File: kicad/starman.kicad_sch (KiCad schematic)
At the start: 202 parts, among them J1 Conn_01x12, J10 Barrel_Jack_MountingPin, J2 Conn_01x10, J3 Conn_01x12, J4 Conn_01x06, J5 Conn_02x03_Counter_Clockwise, J6 Conn_01x12, J7 Conn_01x10, J8 Conn_01x12, J9 Conn_01x08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

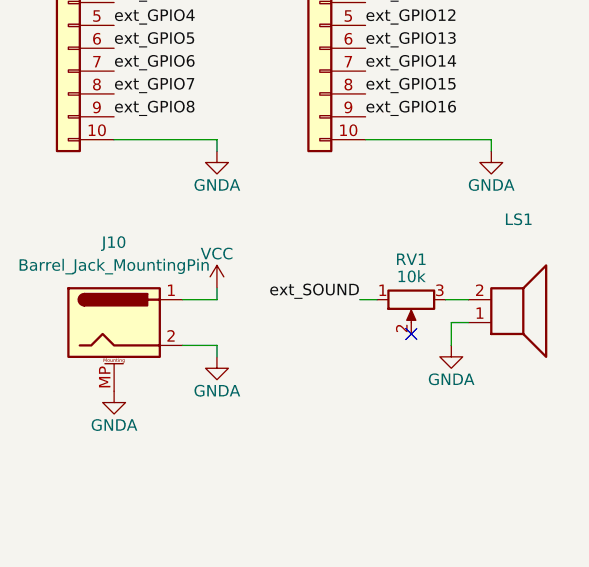
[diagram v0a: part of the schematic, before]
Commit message: Added some neat logos, fixed potentiometer
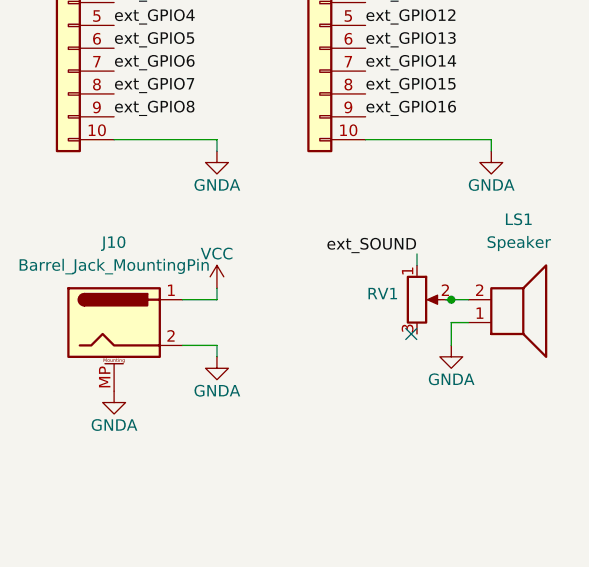
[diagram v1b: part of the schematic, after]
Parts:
- LS1: value (none) -> Speaker; footprint (none) -> Buzzer_Beeper:MagneticBuzzer_StarMicronics_HMB-06_HMB-12
- RV1: value 10k -> (none); footprint Potentiometer_SMD:Potentiometer_ACP_CA9-VSMD_Vertical -> (none)
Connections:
- net at LS1.2: now also RV1.2; no longer RV1.3
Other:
- moved on the sheet: RV1
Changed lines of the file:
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@@
   (junction (at 144.78 176.53) (diameter 0) (color 0 0 0 0)
   )
+  (junction (at 412.115 148.59) (diameter 0) (color 0 0 0 0)
+  )
   (junction (at 154.94 87.63) (diameter 0) (color 0 0 0 0)
   )
@@
     (stroke (width 0) (type default) (color 0 0 0 0))
   )
-  (wire (pts (xy 411.48 148.59) (xy 414.02 148.59))
+  (wire (pts (xy 411.48 148.59) (xy 412.115 148.59))
     (stroke (width 0) (type default) (color 0 0 0 0))
   )
@@
     (stroke (width 0) (type default) (color 0 0 0 0))
   )
+  (wire (pts (xy 412.115 148.59) (xy 414.02 148.59))
+    (stroke (width 0) (type default) (color 0 0 0 0))
+  )
   (wire (pts (xy 116.84 73.66) (xy 134.62 73.66))
     (stroke (width 0) (type default) (color 0 0 0 0))
@@
     (stroke (width 0) (type default) (color 0 0 0 0))
   )
+  (wire (pts (xy 408.305 143.51) (xy 408.305 144.78))
+    (stroke (width 0) (type default) (color 0 0 0 0))
+  )
   (wire (pts (xy 151.13 68.58) (xy 151.13 66.04))
     (stroke (width 0) (type default) (color 0 0 0 0))
@@
     (stroke (width 0) (type default) (color 0 0 0 0))
   )
-  (wire (pts (xy 401.955 148.59) (xy 403.86 148.59))
-    (stroke (width 0) (type default) (color 0 0 0 0))
-  )
   (wire (pts (xy 78.74 143.51) (xy 78.74 146.05))
     (stroke (width 0) (type default) (color 0 0 0 0))
@@
     (effects (font (size 1.27 1.27)) (justify left bottom))
   )
-  (label "ext_SOUND" (at 401.955 148.59 180)
+  (label "ext_SOUND" (at 408.305 143.51 180)
     (effects (font (size 1.27 1.27)) (justify right bottom))
   )
@@
     (in_bom yes) (on_board yes) (fields_autoplaced)
     (property "Reference" "LS1" (id 0) (at 419.608 139.7 0))
-    (property "Value" "" (id 1) (at 419.608 142.24 0))
-    (property "Footprint" "" (id 2) (at 419.1 146.05 0)
+    (property "Value" "Speaker" (id 1) (at 419.608 142.24 0))
+    (property "Footprint" "Buzzer_Beeper:MagneticBuzzer_StarMicronics_HMB-06_HMB-12" (id 2) (at 419.1 146.05 0)
       (effects (font (size 1.27 1.27)) hide)
     )
@@
     (pin "1")
   )
-  (symbol (lib_id "Device:R_Potentiometer") (at 407.67 148.59 90) (mirror x) (unit 1)
+  (symbol (lib_id "Device:R_Potentiometer") (at 408.305 148.59 0) (unit 1)
     (in_bom yes) (on_board yes)
-    (property "Reference" "RV1" (id 0) (at 407.67 144.145 90))
-    (property "Value" "10k" (id 1) (at 407.67 146.05 90))
-    (property "Footprint" "Potentiometer_SMD:Potentiometer_ACP_CA9-VSMD_Vertical" (id 2) (at 407.67 148.59 0)
+    (property "Reference" "RV1" (id 0) (at 404.495 147.955 0))
+    (property "Value" "" (id 1) (at 404.495 149.86 0))
+    (property "Footprint" "" (id 2) (at 408.305 148.59 0)
       (effects (font (size 1.27 1.27)) hide)
     )
-    (property "Datasheet" "~" (id 3) (at 407.67 148.59 0)
+    (property "Datasheet" "~" (id 3) (at 408.305 148.59 0)
       (effects (font (size 1.27 1.27)) hide)
     )
@@
     )
     (path "/7bb1d879-2dbb-42dc-ad02-5b95071e74f8"
-      (reference "RV1") (unit 1) (value "10k") (footprint "Potentiometer_SMD:Potentiometer_ACP_CA9-VSMD_Vertical")
+      (reference "RV1") (unit 1) (value "10k") (footprint "Potentiometer_THT:Potentiometer_Bourns_3339P_Vertical")
     )
     (path "/f9c187ec-e110-4704-b585-3f17ccb7e6fc"

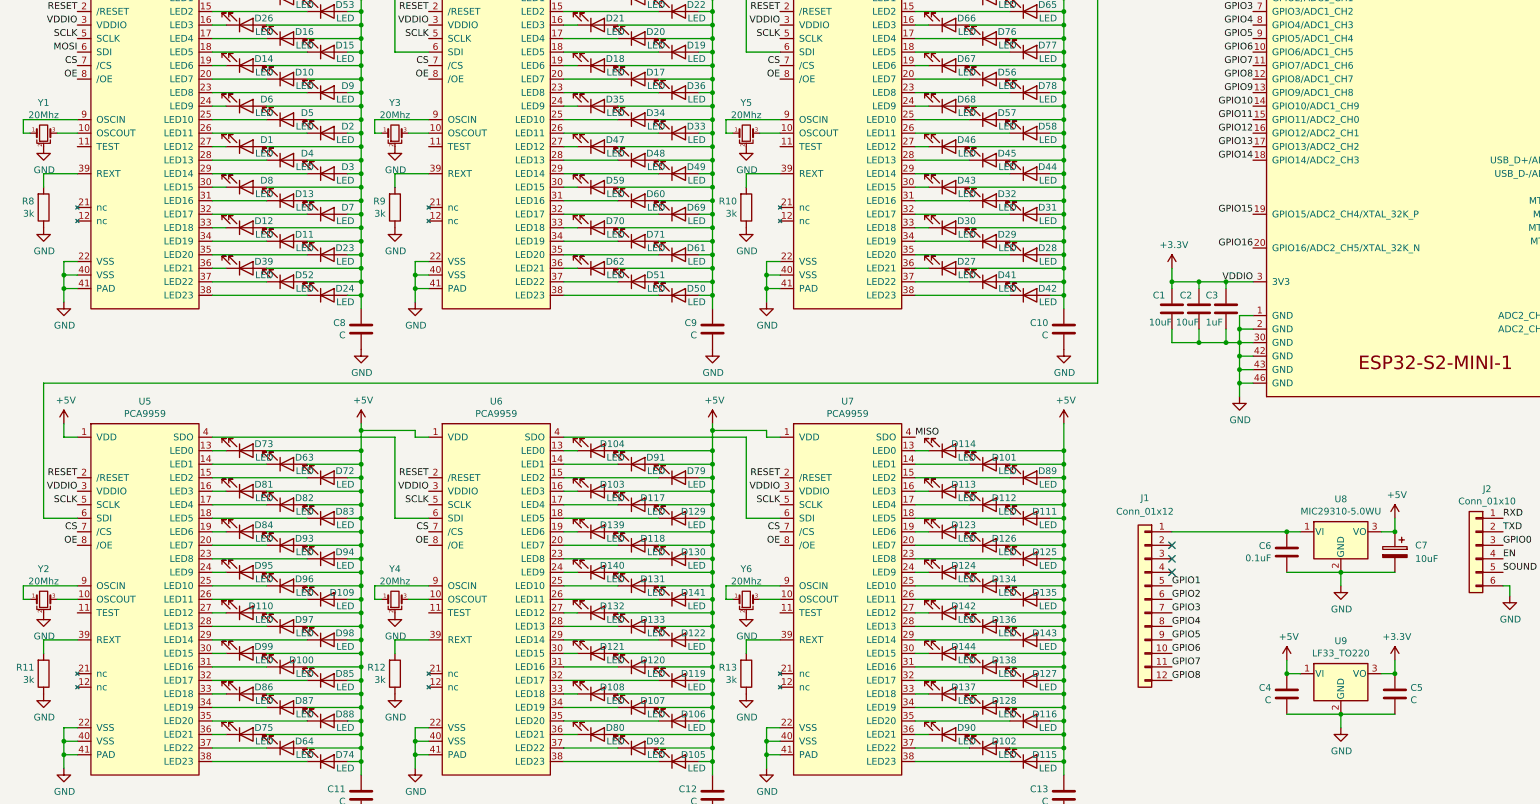
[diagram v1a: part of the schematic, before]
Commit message: Fixed U9 caps, and Y references
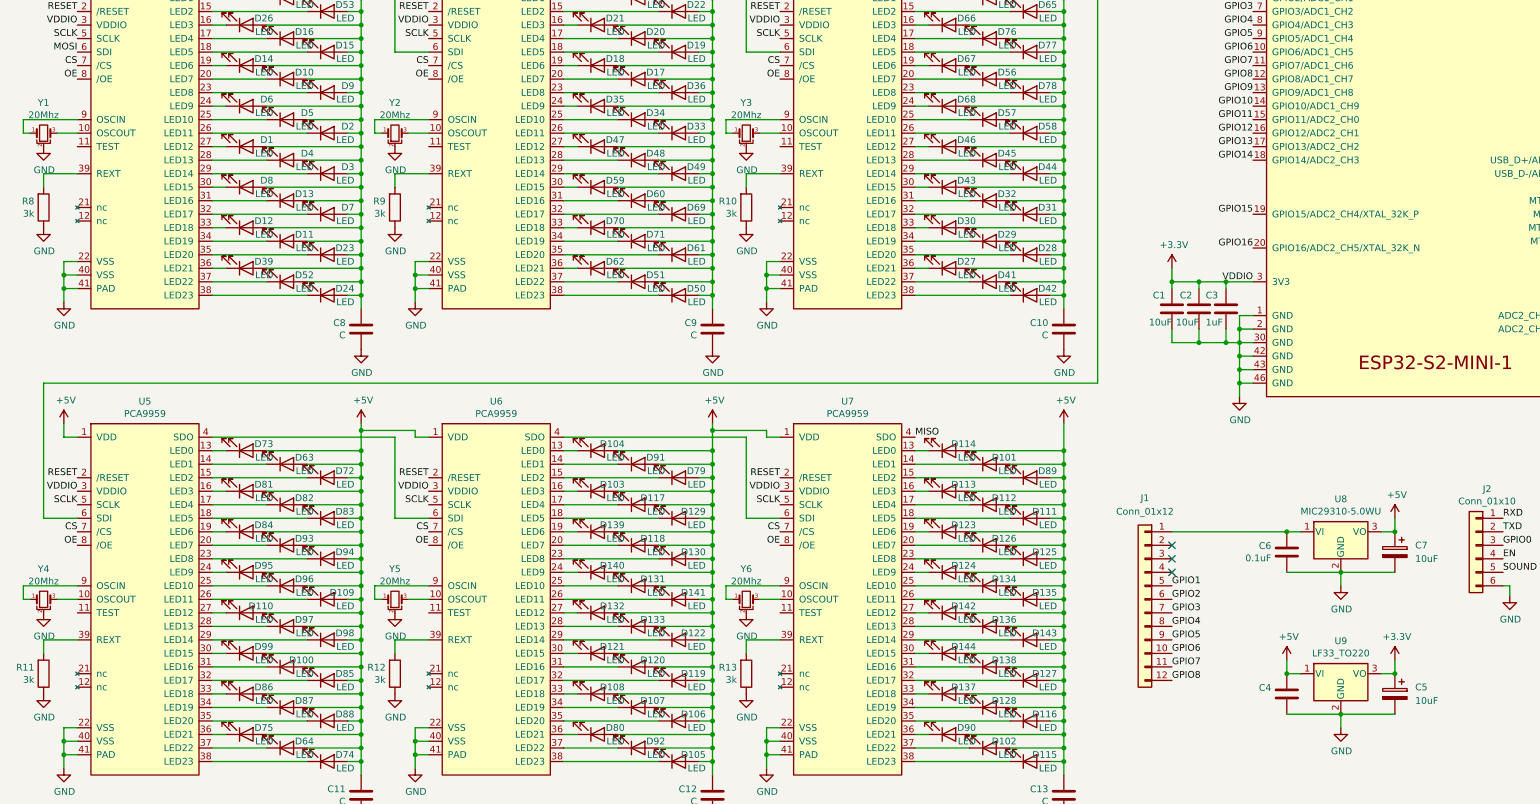
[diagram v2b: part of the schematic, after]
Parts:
- removed C5: C, Capacitor_SMD:C_0805_2012Metric, symbol Device:C
- added C5: 10uF, Capacitor_Tantalum_SMD:CP_EIA-3216-10_Kemet-I, symbol starman-rescue:CP-Device
- C4: value C -> (none)
- renumbered Y3 to Y2, Y5 to Y3, Y2 to Y4, Y4 to Y5
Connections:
- net +3V3: now also C5.1
- net GND: now also C5.2
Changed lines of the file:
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@@
   (junction (at 78.74 26.67) (diameter 0) (color 0 0 0 0)
   )
-  (junction (at 273.05 160.02) (diameter 0) (color 0 0 0 0)
-  )
   (junction (at 144.78 83.82) (diameter 0) (color 0 0 0 0)
   )
@@
   (junction (at 210.82 138.43) (diameter 0) (color 0 0 0 0)
   )
+  (junction (at 273.05 160.02) (diameter 0) (color 0 0 0 0)
+  )
   (junction (at 78.74 135.89) (diameter 0) (color 0 0 0 0)
   )
@@
       (effects (font (size 1.27 1.27)) (justify right))
     )
-    (property "Value" "C" (id 1) (at 249.809 164.973 0)
+    (property "Value" "" (id 1) (at 249.809 164.973 0)
       (effects (font (size 1.27 1.27)) (justify right))
     )
@@
     (pin "1")
   )
-  (symbol (lib_id "Device:C") (at 273.05 163.83 180) (unit 1)
-    (in_bom yes) (on_board yes)
-    (property "Reference" "C5" (id 0) (at 275.971 162.6616 0)
-      (effects (font (size 1.27 1.27)) (justify right))
-    )
-    (property "Value" "C" (id 1) (at 275.971 164.973 0)
-      (effects (font (size 1.27 1.27)) (justify right))
-    )
-    (property "Footprint" "Capacitor_SMD:C_0805_2012Metric" (id 2) (at 272.0848 160.02 0)
-      (effects (font (size 1.27 1.27)) hide)
-    )
-    (property "Datasheet" "~" (id 3) (at 273.05 163.83 0)
-      (effects (font (size 1.27 1.27)) hide)
-    )
-    (pin "1")
-    (pin "2")
-  )
   (symbol (lib_id "Device:LED") (at 130.81 151.13 0) (mirror x) (unit 1)
     (in_bom yes) (on_board yes)
@@
   (symbol (lib_id "Device:Crystal_GND2_Small") (at 19.05 146.05 0) (unit 1)
     (in_bom yes) (on_board yes)
-    (property "Reference" "Y2" (id 0) (at 19.05 140.335 0))
+    (property "Reference" "Y4" (id 0) (at 19.05 140.335 0))
     (property "Value" "20Mhz" (id 1) (at 19.05 142.6464 0))
     (property "Footprint" "Crystal:Resonator_SMD_muRata_CSTxExxV-3Pin_3.0x1.1mm" (id 2) (at 19.05 146.05 0)
@@
   (symbol (lib_id "Device:Crystal_GND2_Small") (at 85.09 146.05 0) (unit 1)
     (in_bom yes) (on_board yes)
-    (property "Reference" "Y4" (id 0) (at 85.09 140.335 0))
+    (property "Reference" "Y5" (id 0) (at 85.09 140.335 0))
     (property "Value" "20Mhz" (id 1) (at 85.09 142.6464 0))
     (property "Footprint" "Crystal:Resonator_SMD_muRata_CSTxExxV-3Pin_3.0x1.1mm" (id 2) (at 85.09 146.05 0)
@@
   (symbol (lib_id "Device:Crystal_GND2_Small") (at 85.09 58.42 0) (unit 1)
     (in_bom yes) (on_board yes)
-    (property "Reference" "Y3" (id 0) (at 85.09 52.705 0))
+    (property "Reference" "Y2" (id 0) (at 85.09 52.705 0))
     (property "Value" "20Mhz" (id 1) (at 85.09 55.0164 0))
     (property "Footprint" "Crystal:Resonator_SMD_muRata_CSTxExxV-3Pin_3.0x1.1mm" (id 2) (at 85.09 58.42 0)
@@
   (symbol (lib_id "Device:Crystal_GND2_Small") (at 151.13 58.42 0) (unit 1)
     (in_bom yes) (on_board yes)
-    (property "Reference" "Y5" (id 0) (at 151.13 52.705 0))
+    (property "Reference" "Y3" (id 0) (at 151.13 52.705 0))
     (property "Value" "20Mhz" (id 1) (at 151.13 55.0164 0))
     (property "Footprint" "Crystal:Resonator_SMD_muRata_CSTxExxV-3Pin_3.0x1.1mm" (id 2) (at 151.13 58.42 0)
@@
     (pin "1")
   )
+  (symbol (lib_id "starman-rescue:CP-Device") (at 273.05 163.83 0) (mirror y) (unit 1)
+    (in_bom yes) (on_board yes)
+    (property "Reference" "C5" (id 0) (at 276.86 162.56 0)
+      (effects (font (size 1.27 1.27)) (justify right))
+    )
+    (property "Value" "10uF" (id 1) (at 276.86 165.1 0)
+      (effects (font (size 1.27 1.27)) (justify right))
+    )
+    (property "Footprint" "Capacitor_Tantalum_SMD:CP_EIA-3216-10_Kemet-I" (id 2) (at 272.0848 167.64 0)
+      (effects (font (size 1.27 1.27)) hide)
+    )
+    (property "Datasheet" "~" (id 3) (at 273.05 163.83 0)
+      (effects (font (size 1.27 1.27)) hide)
+    )
+    (pin "1")
+    (pin "2")
+  )
   (symbol (lib_id "Connector:Barrel_Jack_MountingPin") (at 374.65 151.13 0) (unit 1)
     (in_bom yes) (on_board yes) (fields_autoplaced)
@@
     )
     (path "/00000000-0000-0000-0000-000062ef9b1b"
-      (reference "C4") (unit 1) (value "C") (footprint "Capacitor_SMD:C_0805_2012Metric")
+      (reference "C4") (unit 1) (value "0.1uF") (footprint "Capacitor_SMD:C_0805_2012Metric")
     )
-    (path "/00000000-0000-0000-0000-00006302b30d"
-      (reference "C5") (unit 1) (value "C") (footprint "Capacitor_SMD:C_0805_2012Metric")
+    (path "/b34588a8-1417-4351-ab8d-184680f43c1f"
+      (reference "C5") (unit 1) (value "10uF") (footprint "Capacitor_Tantalum_SMD:CP_EIA-3216-10_Kemet-I")
     )
     (path "/00000000-0000-0000-0000-000062d752a1"
@@
       (reference "Y1") (unit 1) (value "20Mhz") (footprint "Crystal:Resonator_SMD_muRata_CSTxExxV-3Pin_3.0x1.1mm")
     )
-    (path "/00000000-0000-0000-0000-0000657b65ae"
+    (path "/00000000-0000-0000-0000-0000659d43a6"
       (reference "Y2") (unit 1) (value "20Mhz") (footprint "Crystal:Resonator_SMD_muRata_CSTxExxV-3Pin_3.0x1.1mm")
     )
-    (path "/00000000-0000-0000-0000-0000659d43a6"
+    (path "/00000000-0000-0000-0000-000065c01b7e"
       (reference "Y3") (unit 1) (value "20Mhz") (footprint "Crystal:Resonator_SMD_muRata_CSTxExxV-3Pin_3.0x1.1mm")
     )
-    (path "/00000000-0000-0000-0000-00006588ef25"
+    (path "/00000000-0000-0000-0000-0000657b65ae"
       (reference "Y4") (unit 1) (value "20Mhz") (footprint "Crystal:Resonator_SMD_muRata_CSTxExxV-3Pin_3.0x1.1mm")
     )
-    (path "/00000000-0000-0000-0000-000065c01b7e"
+    (path "/00000000-0000-0000-0000-00006588ef25"
       (reference "Y5") (unit 1) (value "20Mhz") (footprint "Crystal:Resonator_SMD_muRata_CSTxExxV-3Pin_3.0x1.1mm")
     )

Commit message: Identify candidates for mounting components
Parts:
- C4: value (none) -> 0.1uF
- J1: value Conn_01x12 -> (none); footprint Connector_PinSocket_2.54mm:PinSocket_1x12_P2.54mm_Vertical_SMD_Pin1Right -> (none)
- J2: value Conn_01x10 -> (none); footprint Connector_PinSocket_2.54mm:PinSocket_1x06_P2.54mm_Vertical_SMD_Pin1Left -> (none)
- J3, J8: value Conn_01x12 -> (none)
- J4: value Conn_01x06 -> (none); footprint Connector_PinHeader_2.54mm:PinHeader_1x06_P2.54mm_Vertical -> (none)
- J6: value Conn_01x12 -> (none); footprint Connector_PinHeader_2.54mm:PinHeader_1x12_P2.54mm_Vertical -> (none); Vendor (none) -> M20-8771246
- J9: value Conn_01x08 -> (none); footprint Connector_PinHeader_2.54mm:PinHeader_1x10_P2.54mm_Vertical -> (none)
- LS1: value Speaker -> (none); footprint Buzzer_Beeper:MagneticBuzzer_StarMicronics_HMB-06_HMB-12 -> (none)
- Y4: value 20Mhz -> (none); footprint Crystal:Resonator_SMD_muRata_CSTxExxV-3Pin_3.0x1.1mm -> (none)
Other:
- moved on the sheet: C14, C15, J10, J4, J5, J6, J7, J8, J9, LS1, R2, R3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

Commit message: Added KiCad and OSHW logos
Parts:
- J1: value (none) -> M20-8771246; footprint (none) -> Connector_PinSocket_2.54mm:PinSocket_1x12_P2.54mm_Vertical_SMD_Pin1Right
- J2: value (none) -> M20-8770646; footprint (none) -> Connector_PinSocket_2.54mm:PinSocket_1x06_P2.54mm_Vertical_SMD_Pin1Left
- J3: value (none) -> M20-8771246
- J4: value (none) -> ESW-106-44-T-S; footprint (none) -> Connector_PinHeader_2.54mm:PinHeader_1x06_P2.54mm_Vertical
- J6: value (none) -> ESW-112-44-T-S; footprint (none) -> Connector_PinHeader_2.54mm:PinHeader_1x12_P2.54mm_Vertical
- J8: value (none) -> ESW-112-44-T-S
- J9: value (none) -> Conn_01x10; footprint (none) -> Connector_PinHeader_2.54mm:PinHeader_1x10_P2.54mm_Vertical
- RV1: value (none) -> 10k; footprint (none) -> Potentiometer_THT:Potentiometer_Bourns_3339P_Vertical
- Y4: value (none) -> 20Mhz; footprint (none) -> Crystal:Resonator_SMD_muRata_CSTxExxV-3Pin_3.0x1.1mm
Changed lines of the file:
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@@
     (in_bom yes) (on_board yes)
     (property "Reference" "Y4" (id 0) (at 19.05 140.335 0))
-    (property "Value" "" (id 1) (at 19.05 142.6464 0))
-    (property "Footprint" "" (id 2) (at 19.05 146.05 0)
+    (property "Value" "20Mhz" (id 1) (at 19.05 142.6464 0))
+    (property "Footprint" "Crystal:Resonator_SMD_muRata_CSTxExxV-3Pin_3.0x1.1mm" (id 2) (at 19.05 146.05 0)
       (effects (font (size 1.27 1.27)) hide)
     )
@@
     (in_bom yes) (on_board yes)
     (property "Reference" "J1" (id 0) (at 226.06 127 0))
-    (property "Value" "" (id 1) (at 226.06 129.54 0))
-    (property "Footprint" "" (id 2) (at 226.06 146.05 0)
+    (property "Value" "M20-8771246" (id 1) (at 226.06 129.54 0))
+    (property "Footprint" "Connector_PinSocket_2.54mm:PinSocket_1x12_P2.54mm_Vertical_SMD_Pin1Right" (id 2) (at 226.06 146.05 0)
       (effects (font (size 1.27 1.27)) hide)
     )
@@
     (in_bom yes) (on_board yes)
     (property "Reference" "J2" (id 0) (at 290.3728 125.2982 0))
-    (property "Value" "" (id 1) (at 290.3728 127.6096 0))
-    (property "Footprint" "" (id 2) (at 288.29 135.89 0)
+    (property "Value" "M20-8770646" (id 1) (at 290.3728 127.6096 0))
+    (property "Footprint" "Connector_PinSocket_2.54mm:PinSocket_1x06_P2.54mm_Vertical_SMD_Pin1Left" (id 2) (at 288.29 135.89 0)
       (effects (font (size 1.27 1.27)) hide)
     )
@@
     (in_bom yes) (on_board yes)
     (property "Reference" "J4" (id 0) (at 399.415 22.225 0))
-    (property "Value" "" (id 1) (at 399.415 24.765 0))
-    (property "Footprint" "" (id 2) (at 397.51 33.655 0)
+    (property "Value" "ESW-106-44-T-S" (id 1) (at 399.415 24.765 0))
+    (property "Footprint" "Connector_PinHeader_2.54mm:PinHeader_1x06_P2.54mm_Vertical" (id 2) (at 397.51 33.655 0)
       (effects (font (size 1.27 1.27)) hide)
     )
@@
     (in_bom yes) (on_board yes)
     (property "Reference" "J9" (id 0) (at 386.715 111.76 0))
-    (property "Value" "" (id 1) (at 386.715 114.3 0))
-    (property "Footprint" "" (id 2) (at 386.715 128.27 0)
+    (property "Value" "Conn_01x10" (id 1) (at 386.715 114.3 0))
+    (property "Footprint" "Connector_PinHeader_2.54mm:PinHeader_1x10_P2.54mm_Vertical" (id 2) (at 386.715 128.27 0)
       (effects (font (size 1.27 1.27)) hide)
     )
@@
     (in_bom yes) (on_board yes)
     (property "Reference" "J6" (id 0) (at 358.775 68.58 0))
-    (property "Value" "" (id 1) (at 358.775 71.12 0))
-    (property "Footprint" "" (id 2) (at 358.775 87.63 0)
+    (property "Value" "ESW-112-44-T-S" (id 1) (at 358.775 71.12 0))
+    (property "Footprint" "Connector_PinHeader_2.54mm:PinHeader_1x12_P2.54mm_Vertical" (id 2) (at 358.775 87.63 0)
       (effects (font (size 1.27 1.27)) hide)
     )
@@
     (in_bom yes) (on_board yes)
     (property "Reference" "RV1" (id 0) (at 393.065 158.115 0))
-    (property "Value" "" (id 1) (at 393.065 160.02 0))
-    (property "Footprint" "" (id 2) (at 396.875 158.75 0)
+    (property "Value" "10k" (id 1) (at 393.065 160.02 0))
+    (property "Footprint" "Potentiometer_THT:Potentiometer_Bourns_3339P_Vertical" (id 2) (at 396.875 158.75 0)
       (effects (font (size 1.27 1.27)) hide)
     )
@@
     (in_bom yes) (on_board yes)
     (property "Reference" "J3" (id 0) (at 314.96 128.27 0))
-    (property "Value" "" (id 1) (at 314.96 130.81 0))
+    (property "Value" "M20-8771246" (id 1) (at 314.96 130.81 0))
     (property "Footprint" "Connector_PinSocket_2.54mm:PinSocket_1x12_P2.54mm_Vertical_SMD_Pin1Left" (id 2) (at 314.96 147.32 0)
       (effects (font (size 1.27 1.27)) hide)
@@
     (in_bom yes) (on_board yes)
     (property "Reference" "J8" (id 0) (at 386.715 68.58 0))
-    (property "Value" "" (id 1) (at 386.715 71.12 0))
+    (property "Value" "ESW-112-44-T-S" (id 1) (at 386.715 71.12 0))
     (property "Footprint" "Connector_PinHeader_2.54mm:PinHeader_1x12_P2.54mm_Vertical" (id 2) (at 386.715 87.63 0)
       (effects (font (size 1.27 1.27)) hide)
